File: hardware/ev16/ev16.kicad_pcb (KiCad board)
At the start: 4 copper layers, 94.4 x 80 mm, 165 parts, among them CN1 Conn_05x02_Female, CN2 PJ-242, J1 USB_C_Receptacle, J10 Conn_02x04_Odd_Even, J11 Conn_02x05_Counter_Clockwise, J2 Conn_01x02_Socket, J3 AudioJack4, J4 Conn_01x18_MountingPin, J5 Conn_02x03_Odd_Even, J7 Conn_02x05_Counter_Clockwise, J8 Conn_02x05_Counter_Clockwise, J9 Conn_02x05_Counter_Clockwise, Q1 2N7002, SW1 SW_SPDT, SW2 SW_Push, SW3 SW_Push, SW4 SW_Push, SW5 SW_Push, U1 BQ21040DBV, U10 STM32F405RGTx, U2 USBLC6-2P6, U3 STM32F072CBTx, U4 CH340C, U5 TPS63060, U6 WM8960CGEFL/RV, U7 ESP32-S3-WROOM-1, U8 M24C02-RMN6TP, U9 BM14B(0.8)-24DS-0.4V(53), Y1 Crystal_GND24

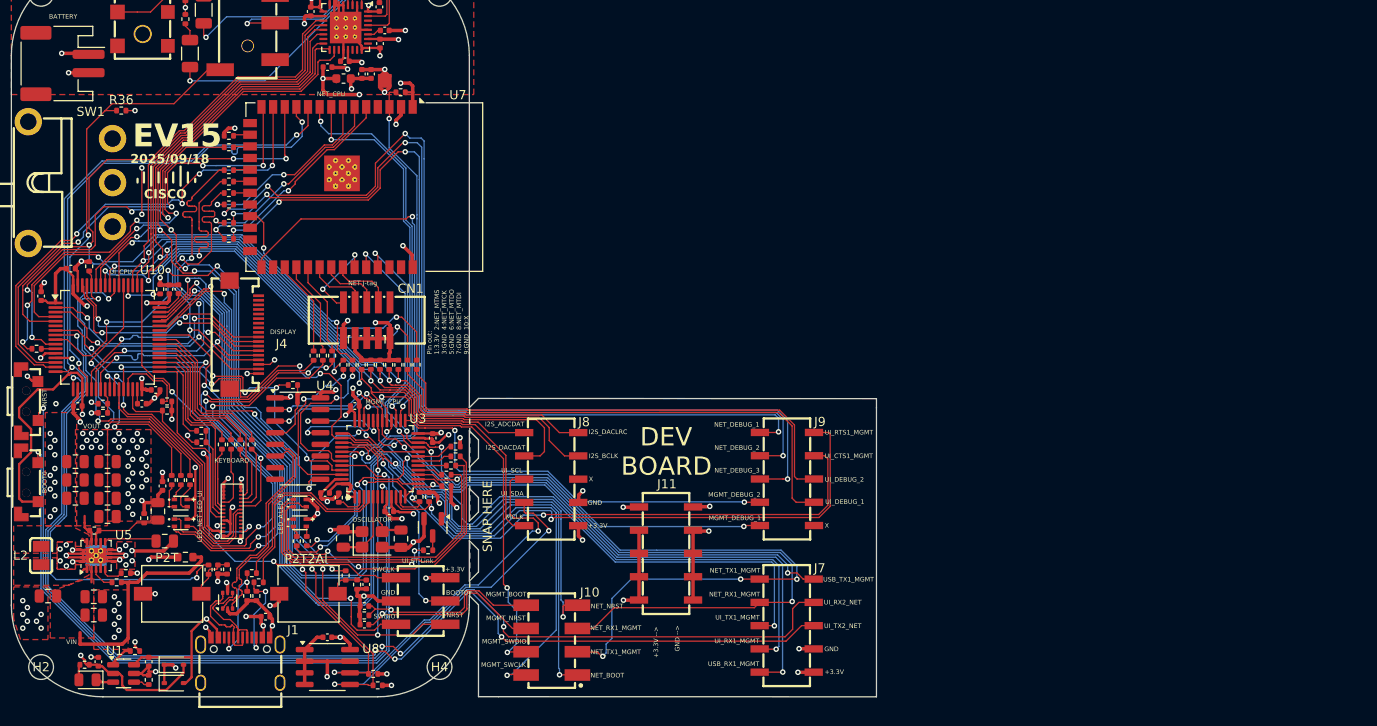
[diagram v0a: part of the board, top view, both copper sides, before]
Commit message: Added a connector for mgmt swdio, added spi to dev board
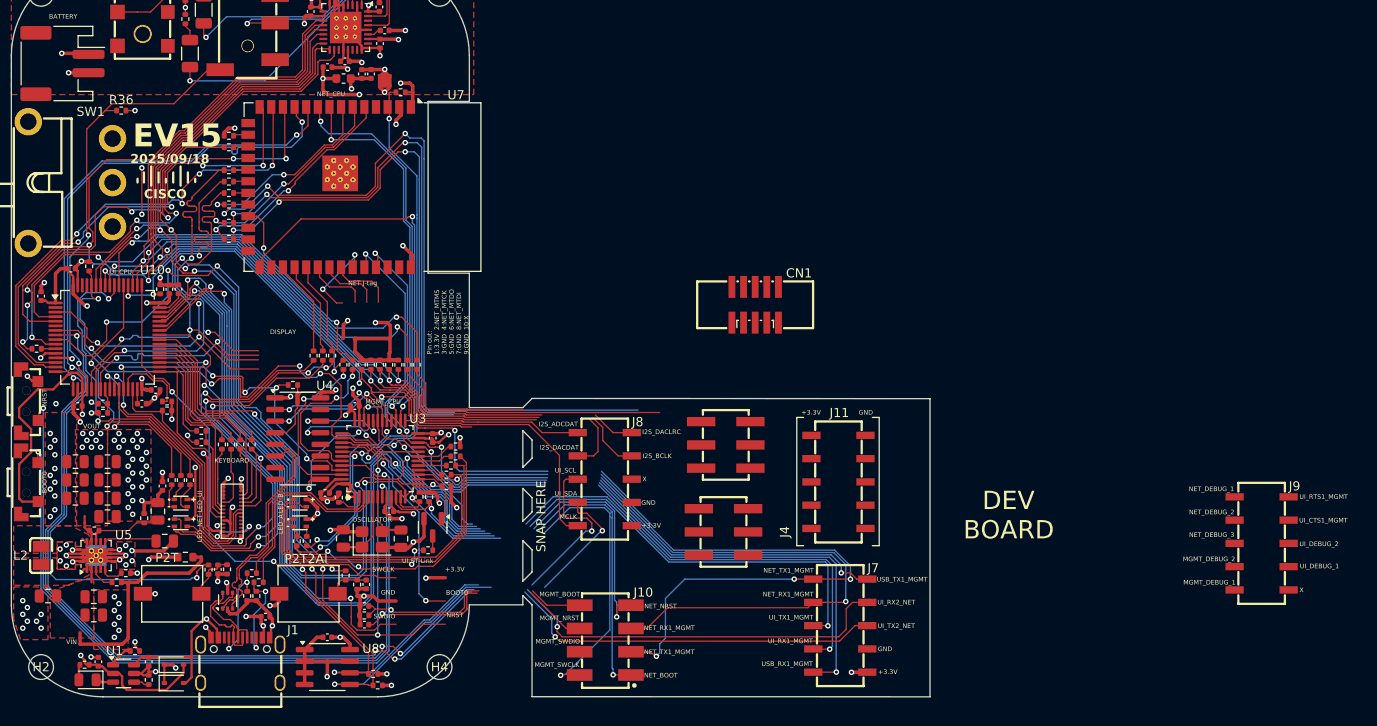
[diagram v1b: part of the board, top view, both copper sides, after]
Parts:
- J4: value Conn_01x18_MountingPin -> Conn_02x03_Odd_Even; footprint Hactar_Footprints:FPC-SMD_18P-P0.50_FPC-0.5-18P-HYH2.0 -> Hactar_Footprints:HDR-SMD_6P-P2.54-V-M-R2-C3-LS7.5-2
- moved J4 56.6 mm to (252.0, 115.0)
- moved J9 52.3 mm to (310.8, 116.3)
- moved CN1 42.4 mm to (255.5, 90.2)
- moved J5 37.4 mm to (252.3, 105.5)
- moved J11 20.4 mm to (264.6, 109.6)
- moved J8 5.85 mm to (239.0, 109.3)
- moved J10 5.85 mm to (239.1, 126.8)
- moved J7 5.85 mm to (264.8, 125.3)
- moved U7 0.20 mm to (212.6, 77.4)
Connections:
- J10 pad 2: /MGMT_SWCLK -> /SPI1_MOSI
- J10 pad 4: /MGMT_SWDIO -> /SPI1_CLK
- J10 pad 6: /MGMT_NRST -> /SPI1_MISO
- J10 pad 8: /MGMT_BOOT -> GND
- J4 pad 1: (no net) -> /MGMT_NRST
- J4 pad 2: (no net) -> /MGMT_SWDIO
- J4 pad 3: (no net) -> /MGMT_BOOT
- J4 pad 4: (no net) -> GND
- J4 pad 5: (no net) -> +3.3V
- J4 pad 6: (no net) -> /MGMT_SWCLK
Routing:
- net GND: track 319.8 -> 243.6 mm, vias 109 -> 104
- net +3.3V: track 251.9 -> 184.1 mm, vias 43 -> 39
- net /UI_RTS1_MGMT: track 140.6 -> 91.5 mm, vias 3 -> 2
- net /UI_CTS1_MGMT: track 133.3 -> 89.4 mm, vias 3 -> 2
- net Net-(J9-Pin_7): track 101.3 -> 58.6 mm, vias 4 -> 3
- net Net-(J9-Pin_6): track 96.8 -> 57.6 mm, vias 4 -> 3
- net Net-(J9-Pin_3): track 53.5 -> 15.4 mm
- net /MGMT_SWCLK: track 53.3 -> 22.2 mm, vias 2 -> 1
- net /SPI1_MOSI: track 49.4 -> 80.6 mm, vias 3 -> 4
- net /MGMT_SWDIO: track 45.9 -> 16.5 mm, vias 4 -> 2
- net /DISP_RST: track 27.7 -> 0.00 mm, vias 2 -> 0
- net Net-(J9-Pin_8): track 108.1 -> 81.9 mm, vias 4 -> 3
- net Net-(J9-Pin_2): track 56.5 -> 31.0 mm
- net /DISP_DC: track 25.0 -> 0.00 mm, vias 2 -> 0
- net /DISP_CS: track 24.1 -> 0.00 mm, vias 2 -> 0
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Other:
- board size 94.4 x 80 mm -> 100.3 x 80 mm
- board text removed: "+3.3V -->"
- board text removed: "GND -->"

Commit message: added volume buttons, changed schematic for buttons to be a 4 lead variant, change led sch to built in ones, picked horizontal leds. Removed one mgmt led. Moved debuggers to dev board. Removed keyboard and screen connectors. Rotated battery connector, added cutout for battery connector. Changed rst and boot buttons to vertical buttons and moved them. Cleaned up usb-c area
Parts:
- removed D4, D6, D8: NH-B1515RGBA-HF, Hactar_Footprints:LED-ARRAY-SMD_4P-L1.6-W1.5-TL_NH-B1515RGBA
- removed H1: MountingHole, MountingHole:MountingHole_2.7mm_M2.5
- removed J10: Conn_02x04_Odd_Even, Hactar_Footprints:HDR-SMD_8P-P2.54-V-M-R2-C4-LS7.4
- removed R47, R48, R51, R52, R53: 680R, Resistor_SMD:R_0402_1005Metric
- removed U9: BM14B(0.8)-24DS-0.4V(53), Hactar_Footprints:BM14B(0.B)-24DS-0.4V(53)
- added C49: 100n, Capacitor_SMD:C_0402_1005Metric, F.Cu at (54.5, 76.8)
- added C50: 100n, Capacitor_SMD:C_0402_1005Metric, F.Cu at (54.5, 77.8)
- added D7: LED_BGAR, Hactar_Footprints:LED-ARRAY-SMD_HS-1204-RGB, F.Cu at (51.6, 64.5)
- added D9: LED_BGAR, Hactar_Footprints:LED-ARRAY-SMD_HS-1204-RGB, F.Cu at (51.6, 68.8)
- added J6: Conn_02x05_Counter_Clockwise, Hactar_Footprints:HDR-SMD_10P-P2.54-V-F-R2-C5-LS7.1-1, F.Cu at (114.8, 102.6)
- added R37: 4k7, Resistor_SMD:R_0402_1005Metric, F.Cu at (54.5, 78.8)
- added SW6: SW_Push, Hactar_Footprints:SW-SMD_SHOU_TS36CA-0.6, F.Cu at (52.0, 77.9)
- added SW7: SW_Push, Hactar_Footprints:SW-SMD_SHOU_TS36CA-0.6, F.Cu at (52.0, 86.8)
- D5: value NH-B1515RGBA-HF -> LED_BGAR
- R17: value 180R -> 1k0
- R23: value 150R -> 4k7
- R24: value 150R -> 1k0
- SW2, SW3: footprint Hactar_Footprints:SW-SMD_SHOU_TS36CA-0.6 -> Hactar_Footprints:KEY-SMD_4P-L4.2-W3.2-P2.20-LS4.6
- SW4, SW5: footprint Hactar_Footprints:SW-SMD_L6.0-W6.0-LS6.6 -> Hactar_Footprints:SW-SMD_4P-L5.1-W5.1-P3.70-LS6.5-TL_H1.5
- moved R3 200.4 mm to (23.2, 86.8), turned to 0 degrees
- moved R23 173.5 mm to (53.2, 70.0), turned to -90 degrees
- moved J9 171.0 mm to (142.3, 86.8)
- moved R16 153.1 mm to (68.8, 81.3), turned to -90 degrees
- moved R19 151.9 mm to (71.0, 81.3), turned to -90 degrees
- moved C38 149.0 mm to (66.8, 81.3), turned to -90 degrees
- moved R56 148.1 mm to (50.5, 72.0), turned to 90 degrees
- moved U8 146.7 mm to (68.8, 86.0), turned to 90 degrees
- moved R59 145.2 mm to (52.5, 72.0), turned to 90 degrees
- moved R60 145.2 mm to (51.5, 72.0), turned to 90 degrees
- moved C47 144.0 mm to (73.0, 87.3), turned to 180 degrees
- moved R62 143.2 mm to (73.0, 86.3), turned to 0 degrees
- moved R17 143.1 mm to (69.8, 73.8), turned to 0 degrees
- moved R22 143.0 mm to (80.1, 70.9)
- moved R24 142.4 mm to (69.8, 72.8), turned to 0 degrees
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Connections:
- net /KB_ROW7 renamed Net-(U10-PB11)
- D5 pad 1: Net-(D5---Pad1) -> Net-(D5-RK)
- D5 pad 3: Net-(D5---Pad3) -> Net-(D5-BK)
- D5 pad 4: Net-(D5---Pad4) -> Net-(D5-GK)
- R15 pad 1: Net-(D4---Pad3) -> Net-(D5-BK)
- R17 pad 1: Net-(D5---Pad3) -> /VOLUME+
- R17 pad 2: /LEDB_B -> Net-(C49-Pad1)
- R20 pad 1: Net-(D4---Pad1) -> Net-(D5-RK)
- R21 pad 1: Net-(D4---Pad4) -> Net-(D5-GK)
- R23 pad 1: Net-(D5---Pad1) -> GND
- R23 pad 2: /LEDB_R -> Net-(C49-Pad1)
- R24 pad 1: /LEDB_G -> /VOLUME-
- R24 pad 2: Net-(D5---Pad4) -> Net-(C50-Pad1)
- R43 pad 2: /KB_COL1 -> Net-(U10-PB13)
- SW2 pad 2: /MGMT_BOOT -> +3.3V
- SW2 pad 3: (no net) -> /MGMT_BOOT
- SW2 pad 4: (no net) -> /MGMT_BOOT
- SW3 pad 2: GND -> /MGMT_NRST
- SW3 pad 3: (no net) -> GND
- SW3 pad 4: (no net) -> GND
- SW4 pad 2: Net-(C46-Pad1) -> +3.3V
- SW5 pad 2: Net-(C47-Pad1) -> +3.3V
- U10 pad 2: /DISP_RST -> unconnected-(U10-PC13-Pad2)
- U10 pad 26: /KB_ROW5 -> unconnected-(U10-PB0-Pad26)
- U10 pad 27: /KB_ROW6 -> unconnected-(U10-PB1-Pad27)
- U10 pad 3: /DISP_BL -> unconnected-(U10-PC14-Pad3)
- U10 pad 33: /KB_ROW1 -> unconnected-(U10-PB12-Pad33)
- U10 pad 35: /KB_ROW2 -> /VOLUME+
- U10 pad 36: Net-(U10-PB15) -> /VOLUME-
- U10 pad 37: Net-(U10-PC6) -> unconnected-(U10-PC6-Pad37)
- U10 pad 38: Net-(U10-PC7) -> unconnected-(U10-PC7-Pad38)
- U10 pad 39: /KB_ROW3 -> unconnected-(U10-PC8-Pad39)
- U10 pad 40: Net-(U10-PC9) -> unconnected-(U10-PC9-Pad40)
- U10 pad 41: /KB_ROW4 -> unconnected-(U10-PA8-Pad41)
- U10 pad 61: /DISP_CS -> unconnected-(U10-PB8-Pad61)
- U10 pad 62: /DISP_DC -> unconnected-(U10-PB9-Pad62)
- U3 pad 18: /LEDB_R -> unconnected-(U3-PB0-Pad18)
- U3 pad 28: /LEDB_B -> unconnected-(U3-PB15-Pad28)
- U3 pad 42: /LEDB_G -> unconnected-(U3-PB6-Pad42)
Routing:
- net /MCLK: track 139.0 -> 4.51 mm, vias 2 -> 1
- net /UI_TX1_MGMT: track 127.2 -> 0.00 mm, vias 4 -> 0
- net /UI_RX1_MGMT: track 125.8 -> 0.00 mm, vias 4 -> 0
- net /UI_TX2_NET: track 174.6 -> 56.6 mm, vias 5 -> 4
- net /UI_RX2_NET: track 175.2 -> 57.4 mm, vias 5 -> 4
- net /NET_TX1_MGMT: track 107.0 -> 0.00 mm, vias 6 -> 0
- net /NET_RX1_MGMT: track 103.5 -> 0.00 mm, vias 4 -> 0
- net /NET_BOOT: track 101.0 -> 0.00 mm, vias 3 -> 0
- net /UI_SDA1: track 145.2 -> 45.8 mm, vias 6 -> 2
- net /UI_SCL1: track 144.7 -> 46.3 mm, vias 6 -> 2
- net /MGMT_BOOT: track 98.3 -> 4.20 mm, vias 3 -> 0
- net /MGMT_NRST: track 96.9 -> 4.20 mm, vias 3 -> 0
- net /UI_RTS1_MGMT: track 91.5 -> 0.00 mm, vias 2 -> 0
- net /NET_NRST: track 90.3 -> 0.00 mm, vias 3 -> 0
- net /UI_CTS1_MGMT: track 89.4 -> 0.00 mm, vias 2 -> 0
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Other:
- board size 100.3 x 80 mm -> 109.8 x 80 mm
- board text added: "EV16"
- board text added: "MGMT BOOT"
- board text added: "MGMT RST"
- board text added: "MGMT STLINK"
- board text added: "SPI1_CLK"
- board text added: "SPI1_MISO"
- board text added: "SPI1_MOSI"
- board text added: "Sense Resistor"
- board text added: "UI STLINK"
- board text removed: "DISPLAY"
- board text removed: "EV15"
- board text removed: "KEYBOARD"
- board text removed: "LED_A"
- board text removed: "LED_B"
- board text removed: "LED_NET"
- board text removed: "LED_UI"
- board text removed: "NET J-tag"
- board text removed: "P2T"
- board text removed: "P2T2AI"
- board text removed: "UI ST-Link"

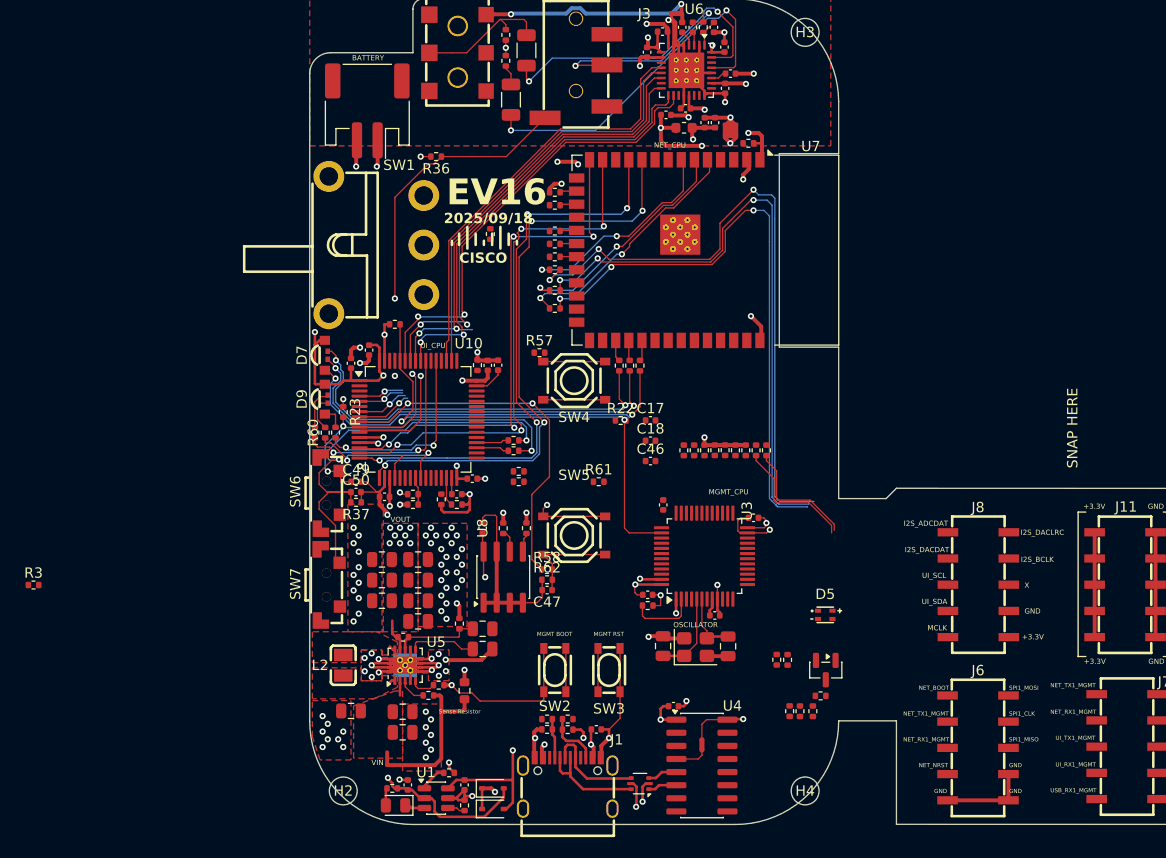
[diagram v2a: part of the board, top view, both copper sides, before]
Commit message: feat: finish tracing all chips, missing dev board
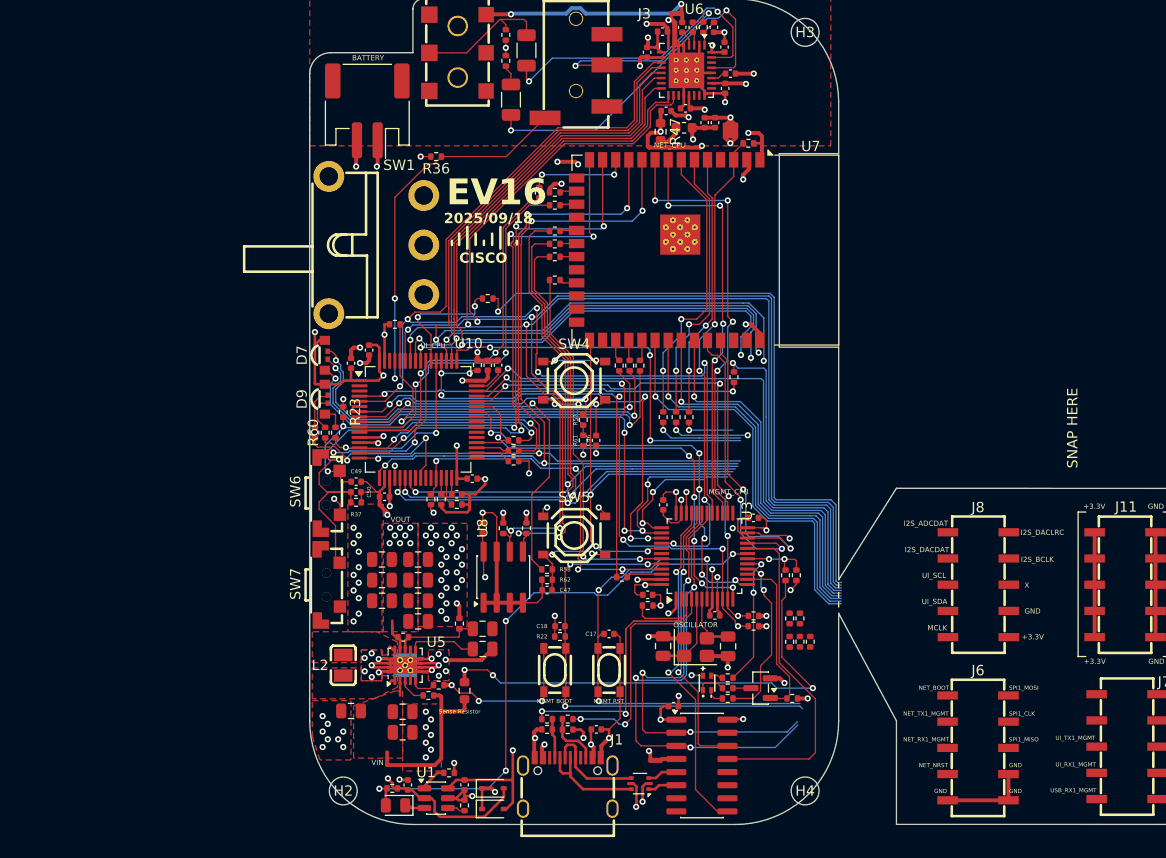
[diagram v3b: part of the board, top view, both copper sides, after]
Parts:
- removed R3: 4k7, Resistor_SMD:R_0402_1005Metric
- added R47: 0R1, Resistor_SMD:R_0603_1608Metric, F.Cu at (84.0, 42.9)
- moved R13 37.8 mm to (97.2, 85.9), turned to -90 degrees
- moved R12 36.9 mm to (96.1, 85.9), turned to -90 degrees
- moved R73 30.7 mm to (67.2, 59.0), turned to 180 degrees
- moved R22 21.7 mm to (74.2, 91.8)
- moved R4 21.3 mm to (73.7, 57.2), turned to 0 degrees
- moved C17 21.1 mm to (79.0, 91.5)
- moved R66 20.3 mm to (97.5, 92.3)
- moved R68 20.3 mm to (98.5, 92.3)
- moved R64 20.3 mm to (96.5, 92.3)
- moved C18 20.0 mm to (74.2, 90.8)
- moved R72 17.7 mm to (84.2, 70.5), turned to -90 degrees
- moved R69 17.4 mm to (97.5, 90.0), turned to -90 degrees
- moved R71 17.0 mm to (85.5, 70.5), turned to -90 degrees
- moved R67 16.8 mm to (96.5, 90.0), turned to -90 degrees
- moved R70 16.7 mm to (86.8, 70.5), turned to -90 degrees
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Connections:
- D1 pad 2: Net-(D1-A) -> /CHG_FB
- J7 pad 6: /NET_TX1_MGMT -> unconnected-(J7-Pin_6-Pad6)
- J7 pad 7: /NET_RX1_MGMT -> unconnected-(J7-Pin_7-Pad7)
- L1 pad 1: +3.3V -> Net-(L1-Pad1)
- R11 pad 2: Net-(D1-A) -> /CHG_FB
- U10 pad 24: /BATTERY_MON -> unconnected-(U10-PC4-Pad24)
- U3 pad 18: unconnected-(U3-PB0-Pad18) -> /BATTERY_MON
- U3 pad 19: Net-(U3-PB1) -> /CHG_FB
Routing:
- net /MCLK: track 4.51 -> 103.9 mm, vias 1 -> 5
- net /UI_SDA1: track 45.8 -> 141.1 mm, vias 2 -> 5
- net /UI_SCL1: track 46.3 -> 137.2 mm, vias 2 -> 5
- net /SPI1_CLK: track 0.00 -> 64.4 mm, vias 0 -> 2
- net /SPI1_MOSI: track 0.00 -> 61.9 mm, vias 0 -> 2
- net /SPI1_MISO: track 0.00 -> 61.1 mm, vias 0 -> 2
- net /CHG_FB: track 0.00 -> 56.3 mm, vias 0 -> 4
- net /UI_SWDIO: track 0.00 -> 56.2 mm, vias 0 -> 1
- net Net-(J9-Pin_8): track 62.4 -> 8.56 mm, vias 3 -> 1
- net Net-(J9-Pin_6): track 57.6 -> 5.00 mm, vias 3 -> 1
- net Net-(J9-Pin_3): track 11.8 -> 63.0 mm, vias 0 -> 1
- net Net-(J9-Pin_7): track 58.6 -> 7.89 mm, vias 3 -> 2
- net /UI_RTS1_MGMT: track 0.00 -> 49.8 mm, vias 0 -> 5
- net /UI_CTS1_MGMT: track 0.00 -> 49.5 mm, vias 0 -> 5
- net /NET_NRST: track 0.00 -> 45.8 mm, vias 0 -> 4
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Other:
- outline, holes or cut-outs redrawn
